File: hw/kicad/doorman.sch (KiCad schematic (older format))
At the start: 18 parts, among them J1 Ring Detection, J2 Lock, J3 Power Supply, K1 S1A05, Q1 BC337, SW1 Button, U1 WeMos_mini, U2 PC817

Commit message: KiCAD PCB proposal.Minor description changes.
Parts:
- LED1: value LED Green -> Green
- LED2: value LED Red -> Red
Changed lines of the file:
@@
 P 6600 5250
 F 0 "LED1" V 6639 5133 50  0000 R CNN
-F 1 "LED Green" V 6548 5133 50  0000 R CNN
+F 1 "Green" V 6548 5133 50  0000 R CNN
 F 2 "LED_THT:LED_D3.0mm" H 6600 5250 50  0001 C CNN
 F 3 "~" H 6600 5250 50  0001 C CNN
@@
 P 6500 2450
 F 0 "LED2" V 6539 2528 50  0000 L CNN
-F 1 "LED Red" V 6448 2528 50  0000 L CNN
+F 1 "Red" V 6448 2528 50  0000 L CNN
 F 2 "LED_THT:LED_D3.0mm" H 6500 2450 50  0001 C CNN
 F 3 "~" H 6500 2450 50  0001 C CNN

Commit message: New Dorman v 1.0 PCB design.
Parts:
- R1, R2, R3, R4, R5: footprint Resistor_THT:R_Axial_DIN0204_L3.6mm_D1.6mm_P5.08mm_Vertical -> Resistor_THT:R_Axial_DIN0204_L3.6mm_D1.6mm_P7.62mm_Horizontal
- SW1: footprint Button_Switch_SMD:SW_SPST_EVQP0 -> Connector_PinHeader_2.54mm:PinHeader_1x02_P2.54mm_Vertical
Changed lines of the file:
@@
 F 0 "R1" V 7893 4150 50  0000 C CNN
 F 1 "680R" V 7984 4150 50  0000 C CNN
-F 2 "Resistor_THT:R_Axial_DIN0204_L3.6mm_D1.6mm_P5.08mm_Vertical" V 8030 4150 50  0001 C CNN
+F 2 "Resistor_THT:R_Axial_DIN0204_L3.6mm_D1.6mm_P7.62mm_Horizontal" V 8030 4150 50  0001 C CNN
 F 3 "~" H 8100 4150 50  0001 C CNN
 	1    8100 4150
@@
 F 0 "R2" H 6530 4904 50  0000 R CNN
 F 1 "380R" H 6530 4995 50  0000 R CNN
-F 2 "Resistor_THT:R_Axial_DIN0204_L3.6mm_D1.6mm_P5.08mm_Vertical" V 6530 4950 50  0001 C CNN
+F 2 "Resistor_THT:R_Axial_DIN0204_L3.6mm_D1.6mm_P7.62mm_Horizontal" V 6530 4950 50  0001 C CNN
 F 3 "~" H 6600 4950 50  0001 C CNN
 	1    6600 4950
@@
 F 0 "R3" H 6430 2004 50  0000 R CNN
 F 1 "380R" H 6430 2095 50  0000 R CNN
-F 2 "Resistor_THT:R_Axial_DIN0204_L3.6mm_D1.6mm_P5.08mm_Vertical" V 6430 2050 50  0001 C CNN
+F 2 "Resistor_THT:R_Axial_DIN0204_L3.6mm_D1.6mm_P7.62mm_Horizontal" V 6430 2050 50  0001 C CNN
 F 3 "~" H 6500 2050 50  0001 C CNN
 	1    6500 2050
@@
 F 0 "R4" V 6093 3250 50  0000 C CNN
 F 1 "1k" V 6184 3250 50  0000 C CNN
-F 2 "Resistor_THT:R_Axial_DIN0204_L3.6mm_D1.6mm_P5.08mm_Vertical" V 6230 3250 50  0001 C CNN
+F 2 "Resistor_THT:R_Axial_DIN0204_L3.6mm_D1.6mm_P7.62mm_Horizontal" V 6230 3250 50  0001 C CNN
 F 3 "~" H 6300 3250 50  0001 C CNN
 	1    6300 3250
@@
 F 0 "R5" V 6143 4700 50  0000 C CNN
 F 1 "1k" V 6234 4700 50  0000 C CNN
-F 2 "Resistor_THT:R_Axial_DIN0204_L3.6mm_D1.6mm_P5.08mm_Vertical" V 6280 4700 50  0001 C CNN
+F 2 "Resistor_THT:R_Axial_DIN0204_L3.6mm_D1.6mm_P7.62mm_Horizontal" V 6280 4700 50  0001 C CNN
 F 3 "~" H 6350 4700 50  0001 C CNN
 	1    6350 4700
@@
 F 0 "SW1" H 4750 5535 50  0000 C CNN
 F 1 "Button" H 4750 5444 50  0000 C CNN
-F 2 "Button_Switch_SMD:SW_SPST_EVQP0" H 4750 5450 50  0001 C CNN
+F 2 "Connector_PinHeader_2.54mm:PinHeader_1x02_P2.54mm_Vertical" H 4750 5450 50  0001 C CNN
 F 3 "~" H 4750 5450 50  0001 C CNN
 	1    4750 5250

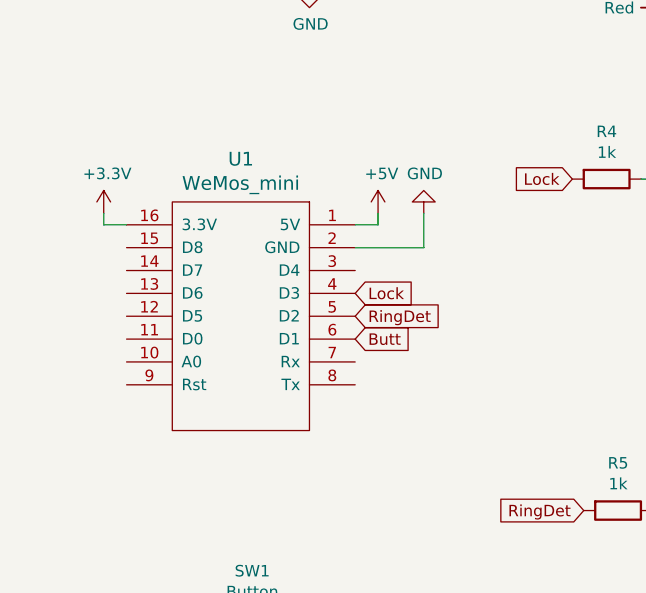
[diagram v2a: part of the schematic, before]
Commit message: First relase of redesign PCB because of wrong ESP module layout. Partialy fix #2
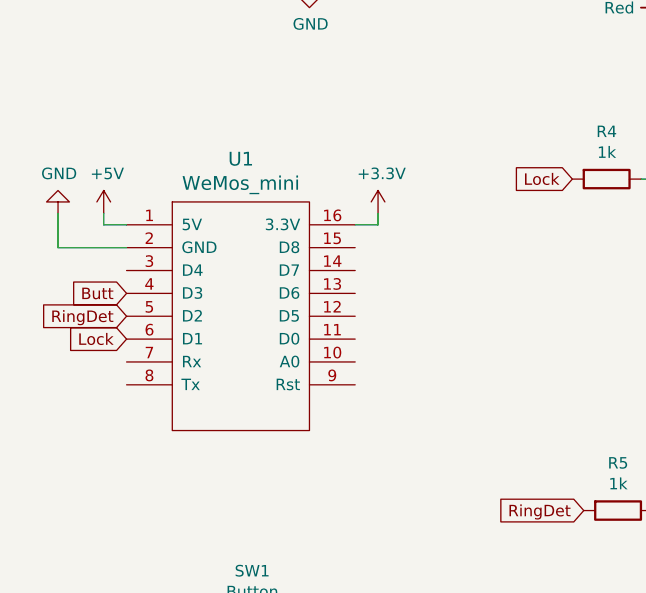
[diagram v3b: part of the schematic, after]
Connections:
- net Butt: now also U1.4 (D3); no longer U1.6 (D1)
- net Lock: now also U1.6 (D1); no longer U1.4 (D3)
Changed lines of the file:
@@
 $EndDescr
-$Comp
-L wemos_mini:WeMos_mini U1
-U 1 1 5E1CE043
-P 4700 3800
-F 0 "U1" H 4700 4437 60  0000 C CNN
-F 1 "WeMos_mini" H 4700 4331 60  0000 C CNN
-F 2 "Module:WEMOS_D1_mini_light" H 5250 3100 60  0001 C CNN
-F 3 "" H 4700 4331 60  0001 C CNN
-	1    4700 3800
-	-1   0    0    -1
-$EndComp
 $Comp
 L Transistor_BJT:BC337 Q1
@@
 L power:+3.3V #PWR0102
 U 1 1 5E207504
+P 5300 3400
+F 0 "#PWR0102" H 5300 3250 50  0001 C CNN
+F 1 "+3.3V" H 5315 3573 50  0000 C CNN
+F 2 "" H 5300 3400 50  0001 C CNN
+F 3 "" H 5300 3400 50  0001 C CNN
+	1    5300 3400
+	1    0    0    -1
+$EndComp
+Wire Wire Line
+	4200 3450 4100 3450
+Wire Wire Line
+	4100 3450 4100 3400
+$Comp
+L power:+5V #PWR0103
+U 1 1 5E2086DC
 P 4100 3400
-F 0 "#PWR0102" H 4100 3250 50  0001 C CNN
-F 1 "+3.3V" H 4115 3573 50  0000 C CNN
+F 0 "#PWR0103" H 4100 3250 50  0001 C CNN
+F 1 "+5V" H 4115 3573 50  0000 C CNN
 F 2 "" H 4100 3400 50  0001 C CNN
 F 3 "" H 4100 3400 50  0001 C CNN
@@
 $EndComp
 Wire Wire Line
-	4200 3450 4100 3450
-Wire Wire Line
-	4100 3450 4100 3400
-$Comp
-L power:+5V #PWR0103
-U 1 1 5E2086DC
-P 5300 3400
-F 0 "#PWR0103" H 5300 3250 50  0001 C CNN
-F 1 "+5V" H 5315 3573 50  0000 C CNN
-F 2 "" H 5300 3400 50  0001 C CNN
-F 3 "" H 5300 3400 50  0001 C CNN
-	1    5300 3400
-	1    0    0    -1
-$EndComp
-Wire Wire Line
 	5200 3450 5300 3450
 Wire Wire Line
@@
 L power:GND #PWR0104
 U 1 1 5E2094AF
-P 5500 3400
-F 0 "#PWR0104" H 5500 3150 50  0001 C CNN
-F 1 "GND" H 5505 3227 50  0000 C CNN
-F 2 "" H 5500 3400 50  0001 C CNN
-F 3 "" H 5500 3400 50  0001 C CNN
-	1    5500 3400
+P 3900 3400
+F 0 "#PWR0104" H 3900 3150 50  0001 C CNN
+F 1 "GND" H 3905 3227 50  0000 C CNN
+F 2 "" H 3900 3400 50  0001 C CNN
+F 3 "" H 3900 3400 50  0001 C CNN
+	1    3900 3400
 	1    0    0    1
 $EndComp
@@
 Connection ~ 6600 4700
 Wire Wire Line
-	5200 3550 5500 3550
-Wire Wire Line
-	5500 3550 5500 3400
-Wire Wire Line
 	6600 5400 6600 5550
 Wire Wire Line
@@
 Wire Wire Line
 	5100 5250 5100 5450
-Text GLabel 5200 3750 2    50   Input ~ 0
+Text GLabel 4200 3950 0    50   Input ~ 0
 Lock
-Text GLabel 5200 3850 2    50   Input ~ 0
+Text GLabel 4200 3850 0    50   Input ~ 0
 RingDet
-Text GLabel 5200 3950 2    50   Input ~ 0
+Text GLabel 4200 3750 0    50   Input ~ 0
 Butt
 Text GLabel 6150 3250 0    50   Input ~ 0
@@
 Wire Wire Line
 	8500 4500 8500 4750
+Wire Wire Line
+	4200 3550 3900 3550
+Wire Wire Line
+	3900 3550 3900 3400
+$Comp
+L wemos_mini:WeMos_mini U1
+U 1 1 5E1CE043
+P 4700 3800
+F 0 "U1" H 4700 4437 60  0000 C CNN
+F 1 "WeMos_mini" H 4700 4331 60  0000 C CNN
+F 2 "Module:WEMOS_D1_mini_light" H 5250 3100 60  0001 C CNN
+F 3 "" H 4700 4331 60  0001 C CNN
+	1    4700 3800
+	1    0    0    -1
+$EndComp
 $EndSCHEMATC
